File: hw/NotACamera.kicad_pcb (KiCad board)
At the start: 2 copper layers, 7 parts, among them U1 7555

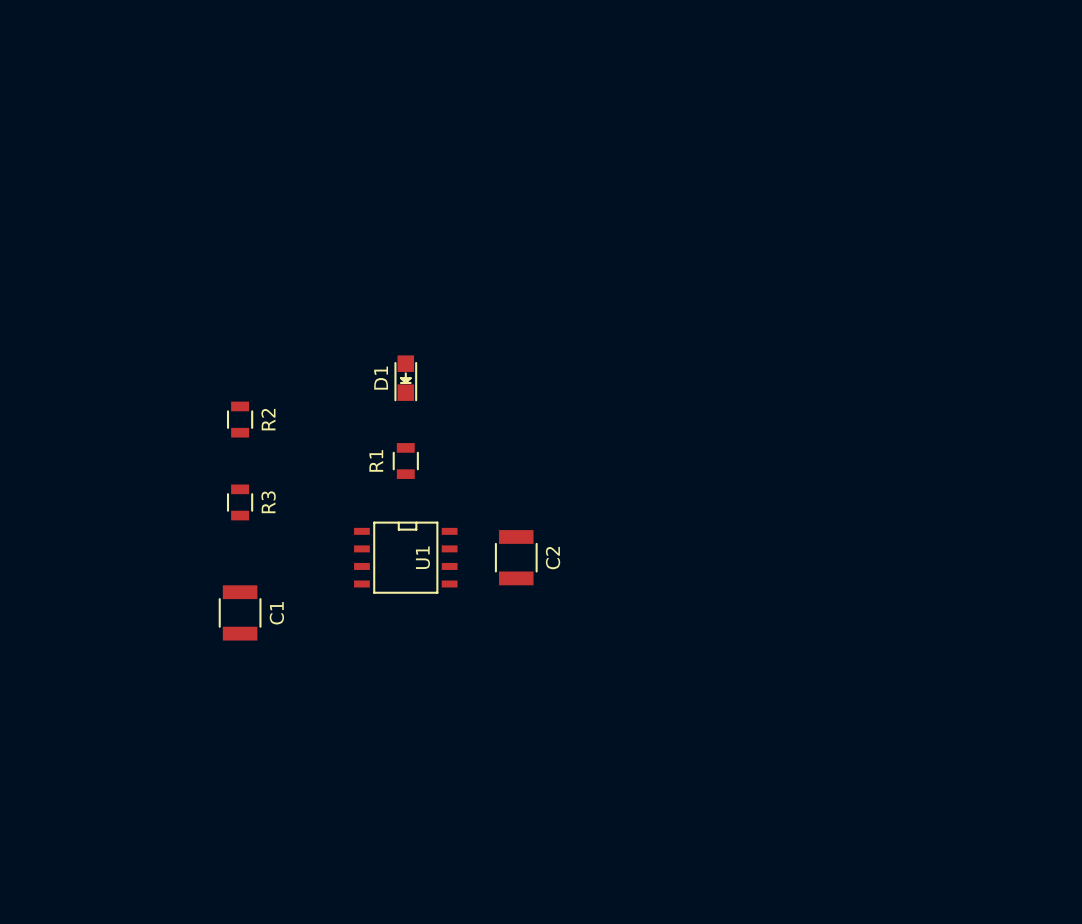
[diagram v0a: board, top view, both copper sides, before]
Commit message: Finished initial layout
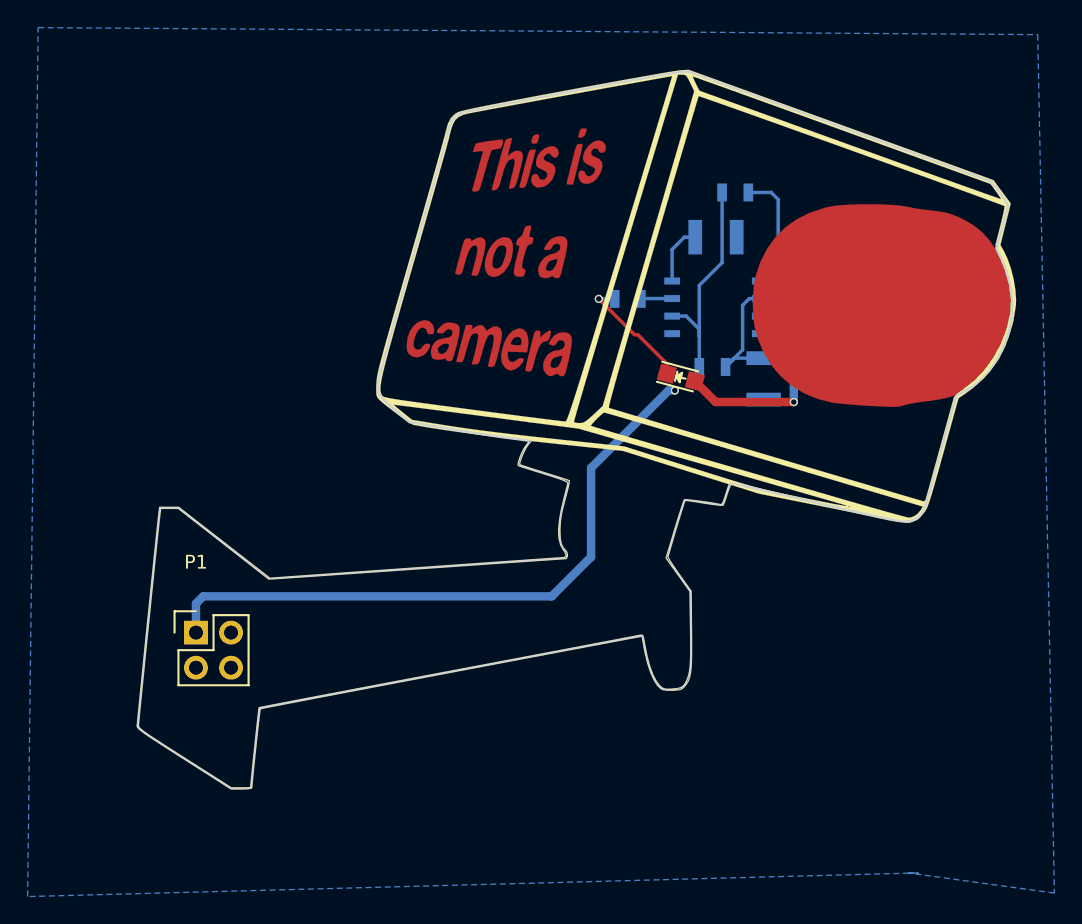
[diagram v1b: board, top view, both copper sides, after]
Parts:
- added CU***: LOGO, NAC:NAC-CU, F.Cu at (114.3, 111.8)
- added EC***: LOGO, NAC:NAC-OL, F.Cu at (114.3, 111.8)
- added G***: LOGO, NAC:NAC-SS, F.Cu at (114.3, 111.8)
- added P1: SAO, Pin_Headers:Pin_Header_Straight_2x02, F.Cu at (86.8, 126.4)
- added SM***: LOGO, NAC:NAC-SM, F.Cu at (114.3, 111.8)
- C1, C2, R1, R2, R3, U1: moved to B.Cu
- moved C1 41.5 mm to (127.9, 108.1)
- moved R2 39.4 mm to (125.9, 94.6), turned to 180 degrees
- moved R3 35.6 mm to (124.2, 107.2), turned to 0 degrees
- moved U1 28.9 mm to (124.5, 102.9), turned to 90 degrees
- moved C2 27.3 mm to (124.5, 97.8), turned to 0 degrees
- moved D1 19.9 mm to (121.9, 108.0), turned to 345 degrees
- moved R1 19.9 mm to (118.1, 102.3), turned to 180 degrees
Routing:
- net /VCC: track 0.00 -> 65.7 mm, vias 0 -> 2
- net Net-(R2-Pad2): track 0.00 -> 16.2 mm
- net Net-(R2-Pad1): track 0.00 -> 11.9 mm
- net Net-(C1-Pad1): track 0.00 -> 9.45 mm
- net Net-(D1-Pad1): track 0.00 -> 8.74 mm, vias 0 -> 1
- net Net-(R1-Pad1): track 0.00 -> 2.27 mm
- added copper zone on B.Cu, net /GND
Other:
- board outline added: 63.4 x 52 mm

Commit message: Implemented inverted lens
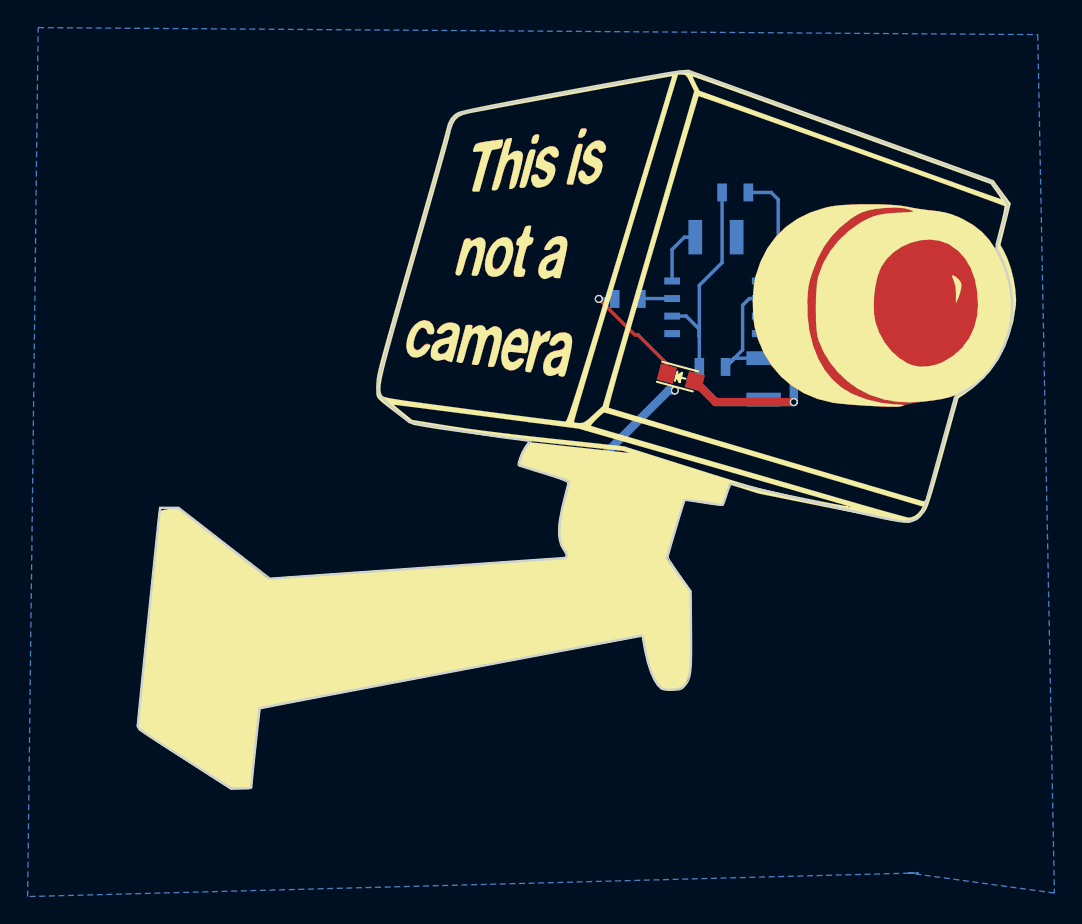
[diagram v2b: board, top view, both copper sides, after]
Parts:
- removed SM***: LOGO, NAC:NAC-SM
- added G***: LOGO, NAC:NAC-SM-invert, F.Cu at (114.3, 111.8)

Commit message: Moved back silk refdes
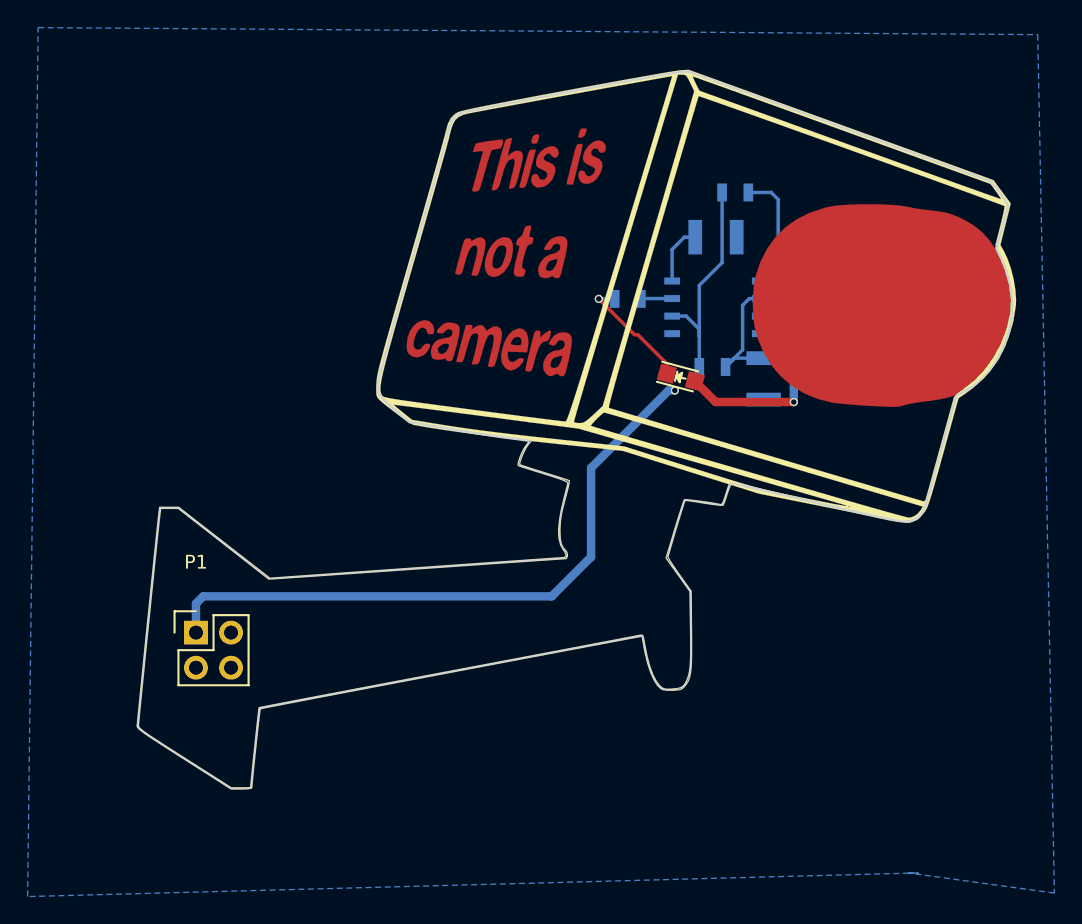
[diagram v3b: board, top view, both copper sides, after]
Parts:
- removed the G*** at (114.3, 111.8)
- added SM***: LOGO, NAC:NAC-SM-invert, F.Cu at (114.3, 111.8)

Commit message: Finalized version of NAC
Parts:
- moved R2 13.1 mm to (125.7, 107.7), turned to 270 degrees
- moved C1 8.29 mm to (119.6, 107.7), turned to 180 degrees
- moved C2 4.83 mm to (119.7, 98.3), turned to 180 degrees
- moved R1 2.32 mm to (119.1, 104.3), turned to 270 degrees
- moved R3 1.17 mm to (123.2, 107.8), turned to 90 degrees
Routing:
- net Net-(R2-Pad1): track 11.9 -> 4.22 mm
- net /VCC: track 65.7 -> 72.4 mm
- net Net-(R2-Pad2): track 16.2 -> 10.1 mm, vias 0 -> 2
- net Net-(D1-Pad1): track 8.74 -> 3.45 mm
- net Net-(R1-Pad1): track 2.27 -> 2.98 mm
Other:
- board text added: "Instructions: https://contextualelectronics.com/NotACamera"

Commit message: Moved / modified back silkscreen
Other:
- board text added: "Instructions: https://contextualelectronics.com/NAC"
- board text removed: "Instructions: https://contextualelectronics.com/NotACamera"
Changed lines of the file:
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@@
     (36 B.SilkS user)
     (37 F.SilkS user)
-    (38 B.Mask user hide)
-    (39 F.Mask user hide)
+    (38 B.Mask user)
+    (39 F.Mask user)
     (40 Dwgs.User user)
     (41 Cmts.User user)
@@
   )
   (setup
-    (last_trace_width 0.6096)
+    (last_trace_width 0.25)
     (user_trace_width 0.6096)
     (trace_clearance 0.2)
@@
       (xy 27.245941 -11.186984) (xy 27.286485 -11.212611) (xy 27.348169 -11.200314)) (layer F.Mask) (width 0.01))
   )
-  (gr_text "Instructions:\nhttps://contextualelectronics.com/NotACamera" (at 120.904 110.744 345) (layer B.SilkS)
+  (gr_text "Instructions:\nhttps://contextualelectronics.com/NAC" (at 125.73 93.726 345) (layer B.SilkS)
     (effects (font (size 1.016 1.016) (thickness 0.2032)) (justify mirror))
   )
